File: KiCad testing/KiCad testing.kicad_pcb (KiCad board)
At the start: 2 copper layers, 101.6 x 127 mm, 44 parts, among them J1 USB_A, Q1 IRF540N, Q2 IRF540N, Q3 IRF540N, Q4 IRF540N, U1 IR2213, U4 IR2213

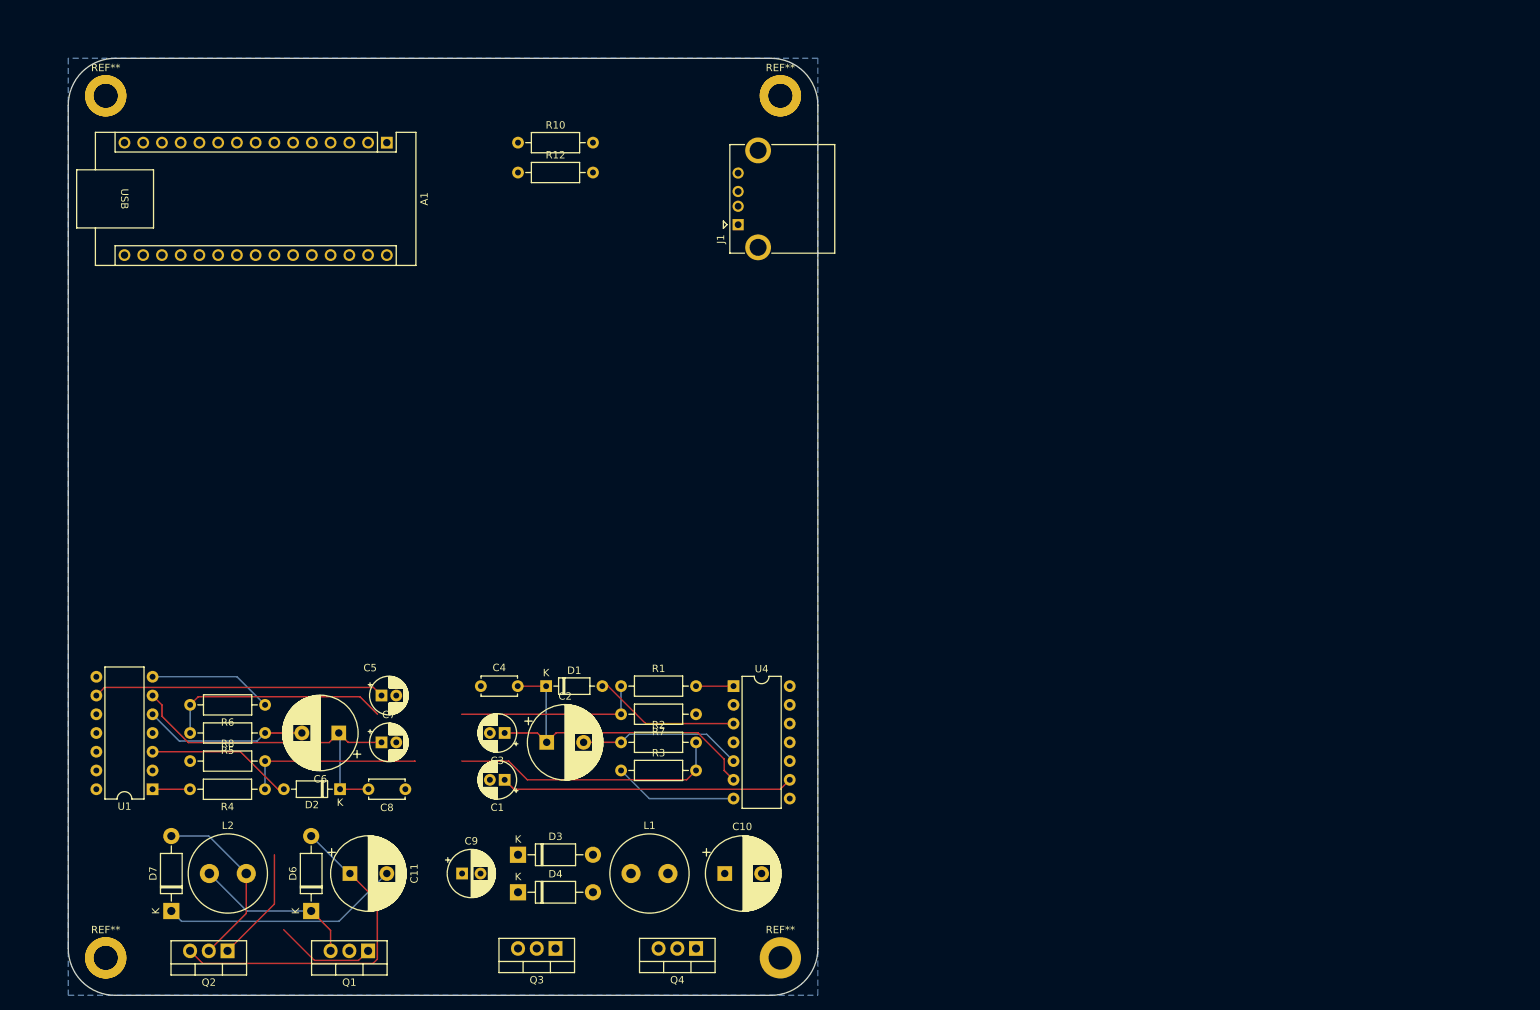
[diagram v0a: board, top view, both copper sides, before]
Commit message: Schematic and PCB Redesign
Double checked all connections in the schematic.
1. Changed the Arduino Nano to an Arduino Uno Rev3
2. Changed the schematic for the two IR2113 nets so that they are more coherent.
3. Added and fixed certain things with the voltage and current sensors
4. Cleaned up the global labels.

Started redesigning the PCB to follow updated schematic and several other constraints.
1. Most power traces are now 1mm trace width to allow more power flow.
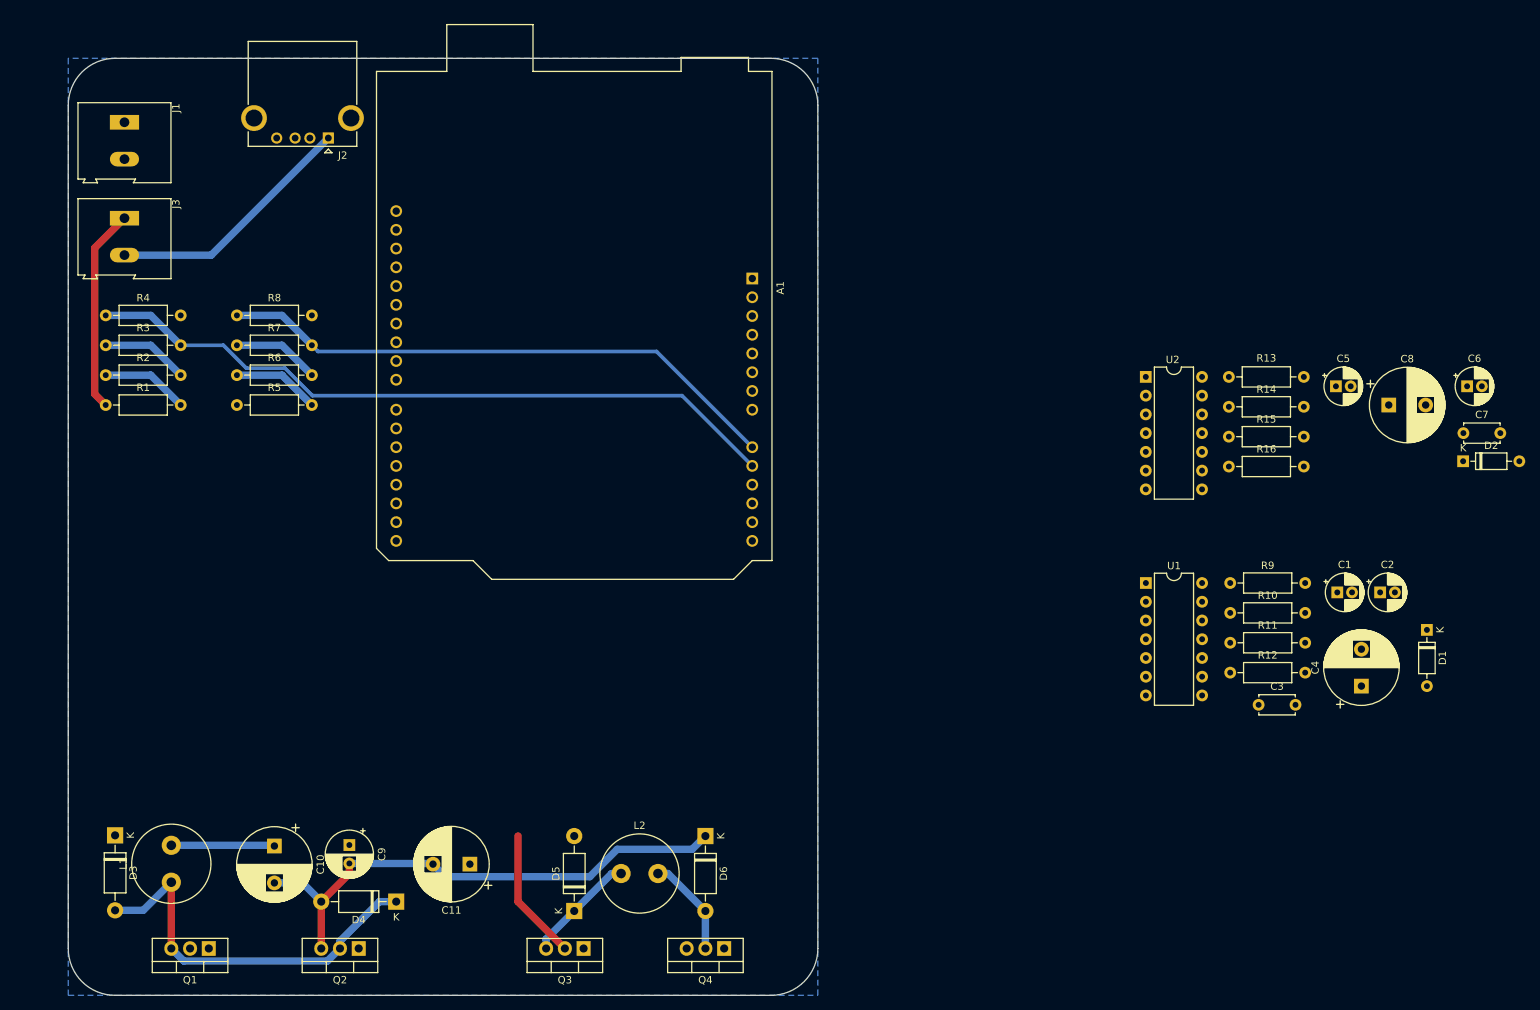
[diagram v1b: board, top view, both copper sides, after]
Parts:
- removed ? (x3): , 
- removed D7: 1N4002, Diode_THT:D_DO-41_SOD81_P10.16mm_Horizontal
- removed REF** (x4): MountingHole_3.2mm_M3_DIN965_Pad, MountingHole:MountingHole_3.2mm_M3_DIN965_Pad
- removed U4: IR2213, Package_DIP:DIP-14_W7.62mm
- added D5: 1N4002, Diode_THT:D_DO-41_SOD81_P10.16mm_Horizontal, F.Cu at (94.0, 141.0)
- added J2: USB_A, Connector_USB:USB_A_CONNFLY_DS1095-WNR0, F.Cu at (60.6, 36.2)
- added J3: Screw_Terminal_01x02, TerminalBlock:TerminalBlock_Altech_AK300-2_P5.00mm, F.Cu at (33.0, 47.1)
- added R11: 10k, Resistor_THT:R_Axial_DIN0207_L6.3mm_D2.5mm_P10.16mm_Horizontal, F.Cu at (182.9, 104.6)
- added R13: 20, Resistor_THT:R_Axial_DIN0207_L6.3mm_D2.5mm_P10.16mm_Horizontal, F.Cu at (182.7, 68.6)
- added R14: 20, Resistor_THT:R_Axial_DIN0207_L6.3mm_D2.5mm_P10.16mm_Horizontal, F.Cu at (182.7, 72.6)
- added R15: 10k, Resistor_THT:R_Axial_DIN0207_L6.3mm_D2.5mm_P10.16mm_Horizontal, F.Cu at (182.7, 76.7)
- added R16: 10k, Resistor_THT:R_Axial_DIN0207_L6.3mm_D2.5mm_P10.16mm_Horizontal, F.Cu at (182.7, 80.7)
- added R9: 20, Resistor_THT:R_Axial_DIN0207_L6.3mm_D2.5mm_P10.16mm_Horizontal, F.Cu at (182.9, 96.5)
- added U2: IR2113, Package_DIP:DIP-14_W7.62mm, F.Cu at (171.4, 68.6)
- A1: value Arduino_Nano_v3.x -> Arduino_UNO_R3; footprint Module:Arduino_Nano -> Module:Arduino_UNO_R3
- C11: value 1000uF -> 100uF
- C2, C6: value 470uF -> 100uF; footprint Capacitor_THT:CP_Radial_D10.0mm_P5.00mm -> Capacitor_THT:CP_Radial_D5.0mm_P2.00mm
- C3, C7: value 100uF -> 100nF; footprint Capacitor_THT:CP_Radial_D5.0mm_P2.00mm -> Capacitor_THT:C_Disc_D4.7mm_W2.5mm_P5.00mm
- C4, C8: value 100nF -> 470uF; footprint Capacitor_THT:C_Disc_D4.7mm_W2.5mm_P5.00mm -> Capacitor_THT:CP_Radial_D10.0mm_P5.00mm
- J1: value USB_A -> Screw_Terminal_01x02; footprint Connector_USB:USB_A_CONNFLY_DS1095-WNR0 -> TerminalBlock:TerminalBlock_Altech_AK300-2_P5.00mm
- R1, R6: value 20 -> 200
- R10: value 1k -> 20
- R12: value 1k -> 10k
- R2, R5: value 10k -> 200
- R3, R4: value 20 -> 1000
- R7, R8: value 10k -> 1000
- U1: value IR2213 -> IR2113
- moved C6 160.0 mm to (215.0, 69.8), turned to 0 degrees
- moved D2 158.6 mm to (214.5, 80.0), turned to 0 degrees
- moved C7 152.5 mm to (214.5, 76.2)
- moved C8 143.1 mm to (204.4, 72.4), turned to 0 degrees
- moved U1 137.5 mm to (171.5, 96.5), turned to 0 degrees
- moved C5 136.0 mm to (197.2, 69.8)
- moved D1 119.6 mm to (209.6, 102.9), turned to -90 degrees
- moved C4 119.4 mm to (200.7, 110.5), turned to 90 degrees
- moved R12 118.0 mm to (182.9, 108.7)
- moved C1 115.7 mm to (197.4, 97.8), turned to 0 degrees
- moved R10 115.7 mm to (182.9, 100.6)
- moved C2 114.8 mm to (203.2, 97.8)
- moved C3 102.3 mm to (186.7, 113.0), turned to 0 degrees
- moved R3 90.6 mm to (30.5, 64.3)
- moved R2 85.8 mm to (30.5, 68.3)
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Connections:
- A1 pad 10: unconnected-(A1-D7-Pad10) -> Battery_Voltage
- A1 pad 11: unconnected-(A1-D8-Pad11) -> PV_Current
- A1 pad 12: PWM_Low -> unconnected-(A1-A3-Pad12)
- A1 pad 13: PWM_High -> unconnected-(A1-SDA/A4-Pad13)
- A1 pad 14: PWM_MPPT -> unconnected-(A1-SCL/A5-Pad14)
- A1 pad 19: Battery_Voltage -> unconnected-(A1-D4-Pad19)
- A1 pad 20: PV_Voltage -> PWM_Low
- A1 pad 21: PV_Current -> PWM_High
- A1 pad 24: unconnected-(A1-A5-Pad24) -> PWM_MPPT_Low
- A1 pad 25: unconnected-(A1-A6-Pad25) -> PWM_MPPT_High
- A1 pad 27: 5V -> unconnected-(A1-D12-Pad27)
- A1 pad 30: 12V -> unconnected-(A1-AREF-Pad30)
- A1 pad 4: GND -> unconnected-(A1-3V3-Pad4)
- A1 pad 5: unconnected-(A1-D2-Pad5) -> 5V
- A1 pad 6: unconnected-(A1-D3-Pad6) -> GND
- A1 pad 7: unconnected-(A1-D4-Pad7) -> GND
- A1 pad 8: unconnected-(A1-D5-Pad8) -> 12V
- A1 pad 9: unconnected-(A1-D6-Pad9) -> PV_Voltage
- C10 pad 1: Battery_V_Sensor -> 12V
- C10 pad 2: +Bidirectional_DCDC_Load -> +Load
- C11 pad 1: -DCDC_Load -> GND
- C11 pad 2: +DCDC_Load -> +Load
- C2 pad 2: VS -> GND
- C4 pad 1: GND -> Net-(D1-K)
- C4 pad 2: Net-(D1-K) -> VS
- C6 pad 2: VS_1 -> GND
- C8 pad 1: GND -> Net-(D2-K)
- C8 pad 2: Net-(D2-K) -> Net-(U2-VS)
- C9 pad 1: -Bidirectional_DCDC_Load -> GND
- C9 pad 2: +Bidirectional_DCDC_Load -> +Load
- D3 pad 1: VS -> GND
- D3 pad 2: +Bidirectional_DCDC_Load -> VS
- D4 pad 1: -Bidirectional_DCDC_Load -> VS
- D4 pad 2: VS -> +Load
- D6 pad 1: Net-(D6-K) -> +Load
- D6 pad 2: -DCDC_Load -> Net-(D6-A)
- J1 pad 1: unconnected-(J1-VBUS-Pad1) -> GND
- J1 pad 2: unconnected-(J1-D--Pad2) -> Net-(J1-Pin_2)
- L1 pad 2: Battery_V_Sensor -> 12V
- L2 pad 1: Net-(D6-K) -> Net-(D5-K)
- L2 pad 2: Net-(D7-A) -> Net-(D6-A)
- Q1 pad 1: Gate_High_1 -> Gate_High
- Q1 pad 2: +PV -> GND
- Q1 pad 3: Net-(D6-K) -> VS
- Q2 pad 1: Gate_Low_1 -> Gate_Low
- Q2 pad 2: Net-(D7-A) -> VS
- Q2 pad 3: -DCDC_Load -> +Load
- Q3 pad 1: Gate_High -> Gate_High_1
- Q3 pad 2: -Bidirectional_DCDC_Load -> +PV
- Q3 pad 3: VS -> Net-(D5-K)
- Q4 pad 1: Gate_Low -> Gate_Low_1
- Q4 pad 2: VS -> Net-(D6-A)
- Q4 pad 3: +Bidirectional_DCDC_Load -> GND
- R1 pad 1: Gate_Low -> 12V
- R1 pad 2: Net-(U4-LO) -> Net-(R1-Pad2)
- R10 pad 1: PV_Voltage -> Gate_Low
- R10 pad 2: GND -> Net-(U1-LO)
- R12 pad 1: Battery_Voltage -> Gate_Low
- R2 pad 1: VS -> Net-(R1-Pad2)
- R2 pad 2: Gate_High -> Net-(R2-Pad2)
- R3 pad 1: Net-(U4-HO) -> Net-(R2-Pad2)
- R3 pad 2: Gate_High -> Battery_Voltage
- R4 pad 1: Gate_Low_1 -> Battery_Voltage
- R4 pad 2: Net-(U1-LO) -> GND
- R5 pad 1: VS_1 -> +PV
- R5 pad 2: Gate_High_1 -> Net-(R5-Pad2)
- R6 pad 1: Net-(U1-HO) -> Net-(R5-Pad2)
- R6 pad 2: Gate_High_1 -> Net-(R6-Pad2)
- R7 pad 1: GND -> Net-(R6-Pad2)
- R7 pad 2: Gate_Low -> PV_Voltage
- R8 pad 1: GND -> PV_Voltage
- R8 pad 2: Gate_Low_1 -> GND
- U1 pad 10: PWM_MPPT -> PWM_High
- U1 pad 12: unconnected-(U1-LIN-Pad12) -> PWM_Low
- U1 pad 5: VS_1 -> VS
- U1 pad 6: Net-(D2-K) -> Net-(D1-K)
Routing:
- net +Load: track 0.00 -> 106.1 mm
- net Battery_Voltage: track 0.00 -> 96.1 mm
- net 5V: track 79.3 -> 0.00 mm
- net PV_Voltage: track 0.00 -> 77.2 mm
- net Net-(D2-K): track 47.2 -> 0.00 mm
- net Net-(D1-K): track 47.1 -> 0.00 mm
- net -DCDC_Load: track 46.8 -> 0.00 mm
- net Gate_High_1: track 44.3 -> 0.00 mm
- net Gate_Low_1: track 39.8 -> 0.00 mm
- net Gate_High: track 37.1 -> 0.00 mm
- net +DCDC_Load: track 32.5 -> 0.00 mm
- net VS: track 22.3 -> 53.3 mm
- net Gate_Low: track 25.4 -> 0.00 mm
- net Net-(D7-A): track 24.9 -> 0.00 mm
- net Net-(D6-K): track 22.4 -> 0.00 mm
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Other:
- board text removed: "Cut outline marks the biggest pcb craftable."

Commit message: Update Schematic
Here the design for the PCB is more or less in a good spot. The gate drivers may get expanded some to take up more room (to make it easier to tell which components go where in the PCB). Most of the traces are placed, though this may change in the future.
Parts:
- moved D1 157.8 mm to (54.6, 132.7), turned to 90 degrees
- moved C4 148.9 mm to (51.9, 104.8), turned to 180 degrees
- moved C2 141.0 mm to (62.2, 100.2), turned to -90 degrees
- moved R10 140.3 mm to (47.0, 135.3), turned to 90 degrees
- moved C1 135.7 mm to (62.2, 109.9), turned to 90 degrees
- moved R12 134.7 mm to (50.8, 135.3), turned to 90 degrees
- moved C3 130.0 mm to (57.1, 102.3), turned to -90 degrees
- moved R11 128.2 mm to (58.4, 135.3), turned to 90 degrees
- moved U1 126.9 mm to (47.0, 121.3), turned to 90 degrees
- moved R9 124.0 mm to (62.2, 125.1), turned to -90 degrees
- moved D2 123.4 mm to (102.9, 132.7), turned to 90 degrees
- moved C7 112.2 mm to (105.4, 102.3), turned to -90 degrees
- moved C8 109.0 mm to (100.3, 104.8), turned to 180 degrees
- moved C6 108.8 mm to (110.5, 100.2), turned to -90 degrees
- moved R14 107.6 mm to (95.2, 135.3), turned to 90 degrees
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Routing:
- net Battery_Voltage: track 96.1 -> 11.8 mm
- net PV_Voltage: track 77.2 -> 11.8 mm
- net Net-(D1-K): track 0.00 -> 45.5 mm
- net Net-(D2-K): track 0.00 -> 45.2 mm
- net VS: track 53.3 -> 95.3 mm
- net Net-(U2-VS): track 0.00 -> 25.0 mm
- net 12V: track 41.6 -> 64.8 mm
- net +Load: track 106.1 -> 87.6 mm
- net +PV: track 17.9 -> 0.00 mm
- net Gate_Low_1: track 0.00 -> 16.2 mm
- net Gate_High: track 0.00 -> 16.2 mm
- net Gate_Low: track 0.00 -> 16.2 mm
- net Gate_High_1: track 0.00 -> 16.2 mm
- net Net-(D5-K): track 15.1 -> 29.0 mm
- net Net-(D6-A): track 13.6 -> 25.1 mm
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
